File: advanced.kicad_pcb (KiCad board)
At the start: 2 copper layers, 29 parts, among them U1 ATtiny24-20P, U2 ATtiny28L-4P, U3 ATtiny13A-P, U4 ATtiny25-20P, U5 ATtiny24-20P, U6 ATtiny85-20P

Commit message: slight progres
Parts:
- removed C7: C_Polarized, Capacitor_THT:CP_Axial_L10.0mm_D4.5mm_P15.00mm_Horizontal
- added  : PinSocket_1x01_P2.54mm_Vertical, Connector_PinSocket_2.54mm:PinSocket_1x01_P2.54mm_Vertical, F.Cu at (189.9, 141.0)
- added  : PinSocket_1x01_P2.54mm_Vertical, Connector_PinSocket_2.54mm:PinSocket_1x01_P2.54mm_Vertical, F.Cu at (222.2, 141.0)
- added  : PinSocket_1x01_P2.54mm_Vertical, Connector_PinSocket_2.54mm:PinSocket_1x01_P2.54mm_Vertical, F.Cu at (163.8, 150.5)
- added  : PinSocket_1x01_P2.54mm_Vertical, Connector_PinSocket_2.54mm:PinSocket_1x01_P2.54mm_Vertical, F.Cu at (117.5, 92.7)
- added  : PinSocket_1x01_P2.54mm_Vertical, Connector_PinSocket_2.54mm:PinSocket_1x01_P2.54mm_Vertical, F.Cu at (136.5, 116.8)
- added  : PinSocket_1x01_P2.54mm_Vertical, Connector_PinSocket_2.54mm:PinSocket_1x01_P2.54mm_Vertical, F.Cu at (166.4, 136.5)
- added  : PinSocket_1x01_P2.54mm_Vertical, Connector_PinSocket_2.54mm:PinSocket_1x01_P2.54mm_Vertical, F.Cu at (101.6, 101.6)
- added  : PinSocket_1x01_P2.54mm_Vertical, Connector_PinSocket_2.54mm:PinSocket_1x01_P2.54mm_Vertical, F.Cu at (146.7, 94.0)
- added  : PinSocket_1x01_P2.54mm_Vertical, Connector_PinSocket_2.54mm:PinSocket_1x01_P2.54mm_Vertical, F.Cu at (183.5, 114.3)
- added  : PinSocket_1x01_P2.54mm_Vertical, Connector_PinSocket_2.54mm:PinSocket_1x01_P2.54mm_Vertical, F.Cu at (221.6, 94.0)
- added  : PinSocket_1x01_P2.54mm_Vertical, Connector_PinSocket_2.54mm:PinSocket_1x01_P2.54mm_Vertical, F.Cu at (233.0, 124.5)
- added  : PinSocket_1x01_P2.54mm_Vertical, Connector_PinSocket_2.54mm:PinSocket_1x01_P2.54mm_Vertical, F.Cu at (215.3, 114.3)
- added  : PinSocket_1x01_P2.54mm_Vertical, Connector_PinSocket_2.54mm:PinSocket_1x01_P2.54mm_Vertical, F.Cu at (141.0, 136.5)
- added  : PinSocket_1x01_P2.54mm_Vertical, Connector_PinSocket_2.54mm:PinSocket_1x01_P2.54mm_Vertical, F.Cu at (143.5, 130.2)
- added  : PinSocket_1x01_P2.54mm_Vertical, Connector_PinSocket_2.54mm:PinSocket_1x01_P2.54mm_Vertical, F.Cu at (128.9, 81.3)
- added  : PinSocket_1x01_P2.54mm_Vertical, Connector_PinSocket_2.54mm:PinSocket_1x01_P2.54mm_Vertical, F.Cu at (167.0, 73.7)
- added  : PinSocket_1x01_P2.54mm_Vertical, Connector_PinSocket_2.54mm:PinSocket_1x01_P2.54mm_Vertical, F.Cu at (129.5, 101.0)
- added  : PinSocket_1x01_P2.54mm_Vertical, Connector_PinSocket_2.54mm:PinSocket_1x01_P2.54mm_Vertical, F.Cu at (153.7, 136.5)
- added  : PinSocket_1x01_P2.54mm_Vertical, Connector_PinSocket_2.54mm:PinSocket_1x01_P2.54mm_Vertical, F.Cu at (101.6, 133.3)
- added  : PinSocket_1x01_P2.54mm_Vertical, Connector_PinSocket_2.54mm:PinSocket_1x01_P2.54mm_Vertical, F.Cu at (262.3, 67.3)
- added  : PinSocket_1x01_P2.54mm_Vertical, Connector_PinSocket_2.54mm:PinSocket_1x01_P2.54mm_Vertical, F.Cu at (220.3, 154.9)
- added  : PinSocket_1x01_P2.54mm_Vertical, Connector_PinSocket_2.54mm:PinSocket_1x01_P2.54mm_Vertical, F.Cu at (172.1, 116.8)
- added  : PinSocket_1x01_P2.54mm_Vertical, Connector_PinSocket_2.54mm:PinSocket_1x01_P2.54mm_Vertical, F.Cu at (192.4, 162.6)
- added  : PinSocket_1x01_P2.54mm_Vertical, Connector_PinSocket_2.54mm:PinSocket_1x01_P2.54mm_Vertical, F.Cu at (160.7, 162.6)
- added  : PinSocket_1x01_P2.54mm_Vertical, Connector_PinSocket_2.54mm:PinSocket_1x01_P2.54mm_Vertical, F.Cu at (140.3, 116.8)
- added  : PinSocket_1x01_P2.54mm_Vertical, Connector_PinSocket_2.54mm:PinSocket_1x01_P2.54mm_Vertical, F.Cu at (121.3, 160.0)
- added  : PinSocket_1x01_P2.54mm_Vertical, Connector_PinSocket_2.54mm:PinSocket_1x01_P2.54mm_Vertical, F.Cu at (178.4, 94.0)
- added  : PinSocket_1x01_P2.54mm_Vertical, Connector_PinSocket_2.54mm:PinSocket_1x01_P2.54mm_Vertical, F.Cu at (198.8, 154.9)
- added  : PinSocket_1x01_P2.54mm_Vertical, Connector_PinSocket_2.54mm:PinSocket_1x01_P2.54mm_Vertical, F.Cu at (189.9, 94.0)
- added  : PinSocket_1x01_P2.54mm_Vertical, Connector_PinSocket_2.54mm:PinSocket_1x01_P2.54mm_Vertical, F.Cu at (135.9, 150.5)
- added  : PinSocket_1x01_P2.54mm_Vertical, Connector_PinSocket_2.54mm:PinSocket_1x01_P2.54mm_Vertical, F.Cu at (150.5, 175.3)
- added  : PinSocket_1x01_P2.54mm_Vertical, Connector_PinSocket_2.54mm:PinSocket_1x01_P2.54mm_Vertical, F.Cu at (118.7, 175.3)
- added  : PinSocket_1x01_P2.54mm_Vertical, Connector_PinSocket_2.54mm:PinSocket_1x01_P2.54mm_Vertical, F.Cu at (130.2, 160.0)
- added  : PinSocket_1x01_P2.54mm_Vertical, Connector_PinSocket_2.54mm:PinSocket_1x01_P2.54mm_Vertical, F.Cu at (262.3, 80.0)
- added  : PinSocket_1x01_P2.54mm_Vertical, Connector_PinSocket_2.54mm:PinSocket_1x01_P2.54mm_Vertical, F.Cu at (108.0, 154.9)
- added  : PinSocket_1x01_P2.54mm_Vertical, Connector_PinSocket_2.54mm:PinSocket_1x01_P2.54mm_Vertical, F.Cu at (143.5, 121.3)
- added  : PinSocket_1x01_P2.54mm_Vertical, Connector_PinSocket_2.54mm:PinSocket_1x01_P2.54mm_Vertical, F.Cu at (87.6, 101.6)
- added  : PinSocket_1x01_P2.54mm_Vertical, Connector_PinSocket_2.54mm:PinSocket_1x01_P2.54mm_Vertical, F.Cu at (211.5, 124.5)
- added  : PinSocket_1x01_P2.54mm_Vertical, Connector_PinSocket_2.54mm:PinSocket_1x01_P2.54mm_Vertical, F.Cu at (137.8, 81.3)
- added  : PinSocket_1x01_P2.54mm_Vertical, Connector_PinSocket_2.54mm:PinSocket_1x01_P2.54mm_Vertical, F.Cu at (108.0, 165.1)
- added  : PinSocket_1x01_P2.54mm_Vertical, Connector_PinSocket_2.54mm:PinSocket_1x01_P2.54mm_Vertical, F.Cu at (205.1, 86.4)
- added  : PinSocket_1x01_P2.54mm_Vertical, Connector_PinSocket_2.54mm:PinSocket_1x01_P2.54mm_Vertical, F.Cu at (87.6, 133.3)
- added  : PinSocket_1x01_P2.54mm_Vertical, Connector_PinSocket_2.54mm:PinSocket_1x01_P2.54mm_Vertical, F.Cu at (103.5, 77.5)
- added  : PinSocket_1x01_P2.54mm_Vertical, Connector_PinSocket_2.54mm:PinSocket_1x01_P2.54mm_Vertical, F.Cu at (196.2, 86.4)
- added  : PinSocket_1x01_P2.54mm_Vertical, Connector_PinSocket_2.54mm:PinSocket_1x01_P2.54mm_Vertical, F.Cu at (167.0, 66.0)
- added  : PinSocket_1x01_P2.54mm_Vertical, Connector_PinSocket_2.54mm:PinSocket_1x01_P2.54mm_Vertical, F.Cu at (129.5, 132.7)
- added  : PinSocket_1x01_P2.54mm_Vertical, Connector_PinSocket_2.54mm:PinSocket_1x01_P2.54mm_Vertical, F.Cu at (212.1, 141.0)
- added  : PinSocket_1x01_P2.54mm_Vertical, Connector_PinSocket_2.54mm:PinSocket_1x01_P2.54mm_Vertical, F.Cu at (262.3, 139.7)
- added REF**: PinSocket_1x07_P2.54mm_Vertical, Connector_PinSocket_2.54mm:PinSocket_1x07_P2.54mm_Vertical, F.Cu at (141.0, 150.5)
- added REF**: PinSocket_1x02_P2.54mm_Vertical, Connector_PinSocket_2.54mm:PinSocket_1x02_P2.54mm_Vertical, F.Cu at (133.4, 136.5)
- added REF**: PinSocket_1x02_P2.54mm_Vertical, Connector_PinSocket_2.54mm:PinSocket_1x02_P2.54mm_Vertical, F.Cu at (117.5, 77.5)
- added REF**: PinSocket_1x02_P2.54mm_Vertical, Connector_PinSocket_2.54mm:PinSocket_1x02_P2.54mm_Vertical, F.Cu at (262.3, 132.1)
- added REF**: PinSocket_1x02_P2.54mm_Vertical, Connector_PinSocket_2.54mm:PinSocket_1x02_P2.54mm_Vertical, F.Cu at (262.3, 72.4)
- added REF**: PinHeader_2x15_P2.54mm_Vertical, Connector_PinHeader_2.54mm:PinHeader_2x15_P2.54mm_Vertical, B.Cu at (274.3, 158.7)
- added REF**: PinSocket_1x03_P2.54mm_Vertical, Connector_PinSocket_2.54mm:PinSocket_1x03_P2.54mm_Vertical, F.Cu at (248.3, 67.3)
- added REF**: PinSocket_1x02_P2.54mm_Vertical, Connector_PinSocket_2.54mm:PinSocket_1x02_P2.54mm_Vertical, F.Cu at (189.9, 146.1)
- added REF**: PinSocket_1x04_P2.54mm_Vertical, Connector_PinSocket_2.54mm:PinSocket_1x04_P2.54mm_Vertical, F.Cu at (248.3, 132.1)
- added REF**: PinSocket_1x04_P2.54mm_Vertical, Connector_PinSocket_2.54mm:PinSocket_1x04_P2.54mm_Vertical, F.Cu at (153.0, 66.0)
- added REF**: PinSocket_1x02_P2.54mm_Vertical, Connector_PinSocket_2.54mm:PinSocket_1x02_P2.54mm_Vertical, F.Cu at (248.3, 77.5)
- added REF**: PinSocket_1x04_P2.54mm_Vertical, Connector_PinSocket_2.54mm:PinSocket_1x04_P2.54mm_Vertical, F.Cu at (103.5, 82.5)
- added REF**: PinSocket_1x02_P2.54mm_Vertical, Connector_PinSocket_2.54mm:PinSocket_1x02_P2.54mm_Vertical, F.Cu at (146.1, 136.5)
- added REF**: PinSocket_1x04_P2.54mm_Vertical, Connector_PinSocket_2.54mm:PinSocket_1x04_P2.54mm_Vertical, F.Cu at (203.8, 141.0)
- moved R11 141.7 mm to (279.4, 86.4), turned to -90 degrees
- moved D1 108.7 mm to (108.0, 158.8), turned to -90 degrees
- moved R6 96.3 mm to (87.6, 104.8), turned to -90 degrees
- moved R10 90.2 mm to (236.2, 64.8), turned to 90 degrees
- moved C8 86.9 mm to (246.6, 111.6), turned to 90 degrees
- moved U1 78.1 mm to (106.7, 77.5)
- moved C2 77.0 mm to (124.5, 160.0)
- moved D4 72.1 mm to (275.6, 67.3)
- moved C5 71.9 mm to (202.1, 154.9)
- moved C6 71.8 mm to (214.8, 124.5)
- moved R3 69.3 mm to (147.3, 175.3), turned to 180 degrees
- moved U5 67.8 mm to (259.1, 80.0), turned to 180 degrees
- moved U2 65.8 mm to (133.4, 147.3), turned to 90 degrees
- moved U3 60.2 mm to (156.2, 66.0)
- moved R1 56.8 mm to (101.6, 104.8), turned to -90 degrees
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
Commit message: a
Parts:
- added  : PinSocket_1x01_P2.54mm_Vertical, Connector_PinSocket_2.54mm:PinSocket_1x01_P2.54mm_Vertical, F.Cu at (281.9, 67.3)
- added  : PinSocket_1x01_P2.54mm_Vertical, Connector_PinSocket_2.54mm:PinSocket_1x01_P2.54mm_Vertical, F.Cu at (279.4, 104.8)
- added  : PinSocket_1x01_P2.54mm_Vertical, Connector_PinSocket_2.54mm:PinSocket_1x01_P2.54mm_Vertical, F.Cu at (246.4, 114.9)
- added  : PinSocket_1x01_P2.54mm_Vertical, Connector_PinSocket_2.54mm:PinSocket_1x01_P2.54mm_Vertical, F.Cu at (236.2, 67.9)
- added  : PinSocket_1x01_P2.54mm_Vertical, Connector_PinSocket_2.54mm:PinSocket_1x01_P2.54mm_Vertical, F.Cu at (209.6, 66.0)
- added  : PinSocket_1x01_P2.54mm_Vertical, Connector_PinSocket_2.54mm:PinSocket_1x01_P2.54mm_Vertical, F.Cu at (246.4, 93.3)
- added  : PinSocket_1x01_P2.54mm_Vertical, Connector_PinSocket_2.54mm:PinSocket_1x01_P2.54mm_Vertical, F.Cu at (236.2, 46.4)
- added  : PinSocket_1x01_P2.54mm_Vertical, Connector_PinSocket_2.54mm:PinSocket_1x01_P2.54mm_Vertical, F.Cu at (271.8, 67.3)
- added  : PinSocket_1x01_P2.54mm_Vertical, Connector_PinSocket_2.54mm:PinSocket_1x01_P2.54mm_Vertical, F.Cu at (279.4, 83.2)
- added  : PinSocket_1x01_P2.54mm_Vertical, Connector_PinSocket_2.54mm:PinSocket_1x01_P2.54mm_Vertical, F.Cu at (199.4, 66.0)
- R1, R10, R11, R2, R3, R4, R5, R6, R7, R8, R9: footprint Resistor_THT:R_Axial_DIN0309_L9.0mm_D3.2mm_P25.40mm_Horizontal -> Resistor_THT:R_Axial_DIN0309_L9.0mm_D3.2mm_P15.24mm_Horizontal
- moved   45.2 mm to (149.2, 175.9)
- moved   43.8 mm to (106.7, 175.9)
- moved R3 43.8 mm to (103.5, 175.9)
- moved   41.2 mm to (62.2, 134.0)
- moved R6 41.2 mm to (62.2, 137.2)
- moved U2 36.4 mm to (99.7, 161.3)
- moved   36.4 mm to (130.2, 164.5)
- moved   36.4 mm to (132.7, 150.5)
- moved   36.4 mm to (107.3, 150.5)
- moved REF** 36.4 mm to (107.3, 164.5)
- moved REF** 36.4 mm to (99.7, 150.5)
- moved   36.4 mm to (120.0, 150.5)
- moved   36.4 mm to (102.2, 164.5)
- moved REF** 36.4 mm to (112.4, 150.5)
- moved R8 35.6 mm to (130.8, 175.9)
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
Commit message: pathing done
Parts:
- removed the   at (138.4, 109.9)
- removed the   at (120.0, 150.5)
- added  : PinSocket_1x01_P2.54mm_Vertical, Connector_PinSocket_2.54mm:PinSocket_1x01_P2.54mm_Vertical, F.Cu at (118.1, 125.1)
- added  : PinSocket_1x01_P2.54mm_Vertical, Connector_PinSocket_2.54mm:PinSocket_1x01_P2.54mm_Vertical, F.Cu at (131.1, 129.0)
- added REF**: PinSocket_1x06_P2.54mm_Vertical, Connector_PinSocket_2.54mm:PinSocket_1x06_P2.54mm_Vertical, F.Cu at (189.9, 154.3)
- added REF**: PinSocket_1x06_P2.54mm_Vertical, Connector_PinSocket_2.54mm:PinSocket_1x06_P2.54mm_Vertical, F.Cu at (133.3, 56.5)
- moved REF** 64.0 mm to (104.8, 87.0)
- moved   52.0 mm to (144.8, 113.7), turned to -90 degrees
- moved   50.4 mm to (104.1, 106.0)
- moved   50.4 mm to (104.1, 127.6)
- moved R6 50.4 mm to (104.1, 109.2)
- moved C2 47.7 mm to (144.8, 116.8), turned to -90 degrees
- moved   44.7 mm to (235.6, 113.7)
- moved   44.7 mm to (235.6, 92.1)
- moved R11 44.7 mm to (235.6, 95.2)
- moved REF** 40.9 mm to (245.7, 129.5)
- moved   40.2 mm to (144.8, 122.6), turned to -90 degrees
- moved   38.1 mm to (247.0, 82.5), turned to -90 degrees
- moved U6 37.6 mm to (214.6, 124.5)
- moved REF** 37.6 mm to (225.4, 124.5)
- moved REF** 37.6 mm to (211.5, 124.5)
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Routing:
- net (no net): track 0.00 -> 2318.0 mm
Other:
- board text added: "GND"
- board text added: "VCC"

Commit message: control components connected
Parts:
- added LED: LED_D5.0mm, LED_THT:LED_D5.0mm, F.Cu at (241.3, 129.5)
- added PIEZO: Buzzer_TDK_PS1240P02BT_D12.2mm_H6.5mm, Buzzer_Beeper:Buzzer_TDK_PS1240P02BT_D12.2mm_H6.5mm, F.Cu at (255.3, 116.3)
- added R (LED): R_Axial_DIN0207_L6.3mm_D2.5mm_P10.16mm_Horizontal, Resistor_THT:R_Axial_DIN0207_L6.3mm_D2.5mm_P10.16mm_Horizontal, F.Cu at (251.5, 134.6)
- added R (PIEZO): R_Axial_DIN0207_L6.3mm_D2.5mm_P10.16mm_Horizontal, Resistor_THT:R_Axial_DIN0207_L6.3mm_D2.5mm_P10.16mm_Horizontal, F.Cu at (264.4, 133.6)
- added RESET: SW_PUSH_6mm_H8.5mm, Button_Switch_THT:SW_PUSH_6mm_H8.5mm, F.Cu at (253.0, 127.8)
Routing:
- net (no net): track 2318.0 -> 2409.2 mm
- net Net-(D4-Pad1): track 0.00 -> 8.58 mm
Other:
- board text added: "+"
- board text added: "-"
- board text added: "ADVANCED"
- board text added: "BOMB ADVANCED"
- board text added: "by phuid & Milda"

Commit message: Add files via upload
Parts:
- moved RESET 5.27 mm to (257.5, 125.0), turned to -90 degrees
- moved PIEZO 4.96 mm to (260.2, 115.6), turned to 180 degrees
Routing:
- net (no net): track 2409.2 -> 2349.1 mm

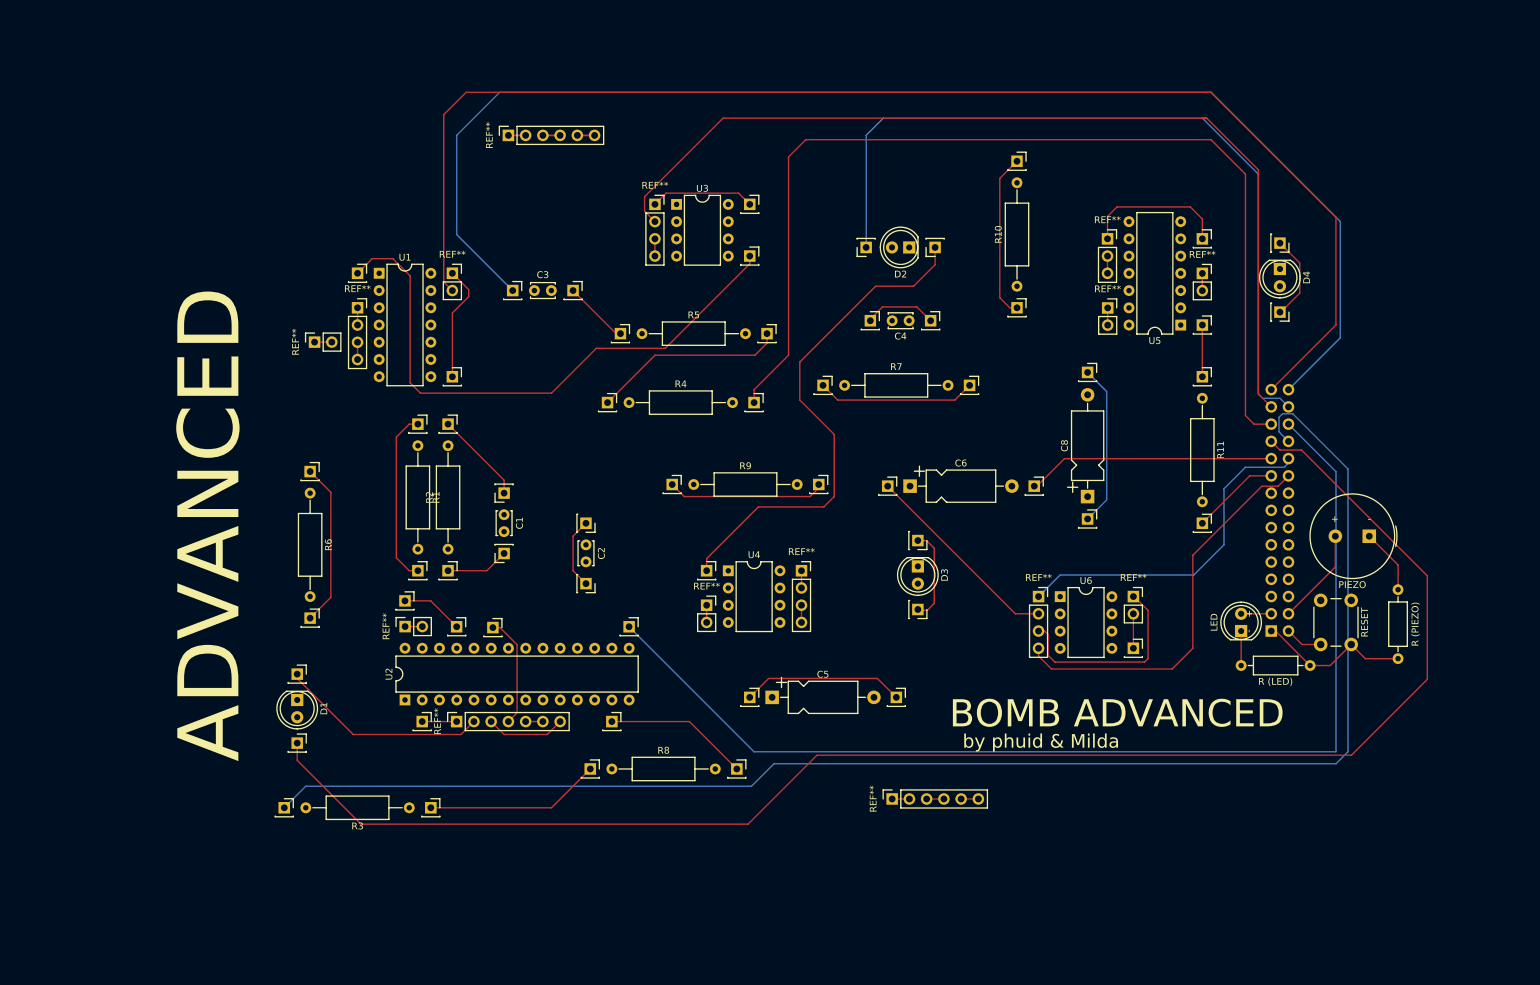
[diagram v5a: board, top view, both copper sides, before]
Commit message: potencio added, not 100% sure, cleanup, clarity changes
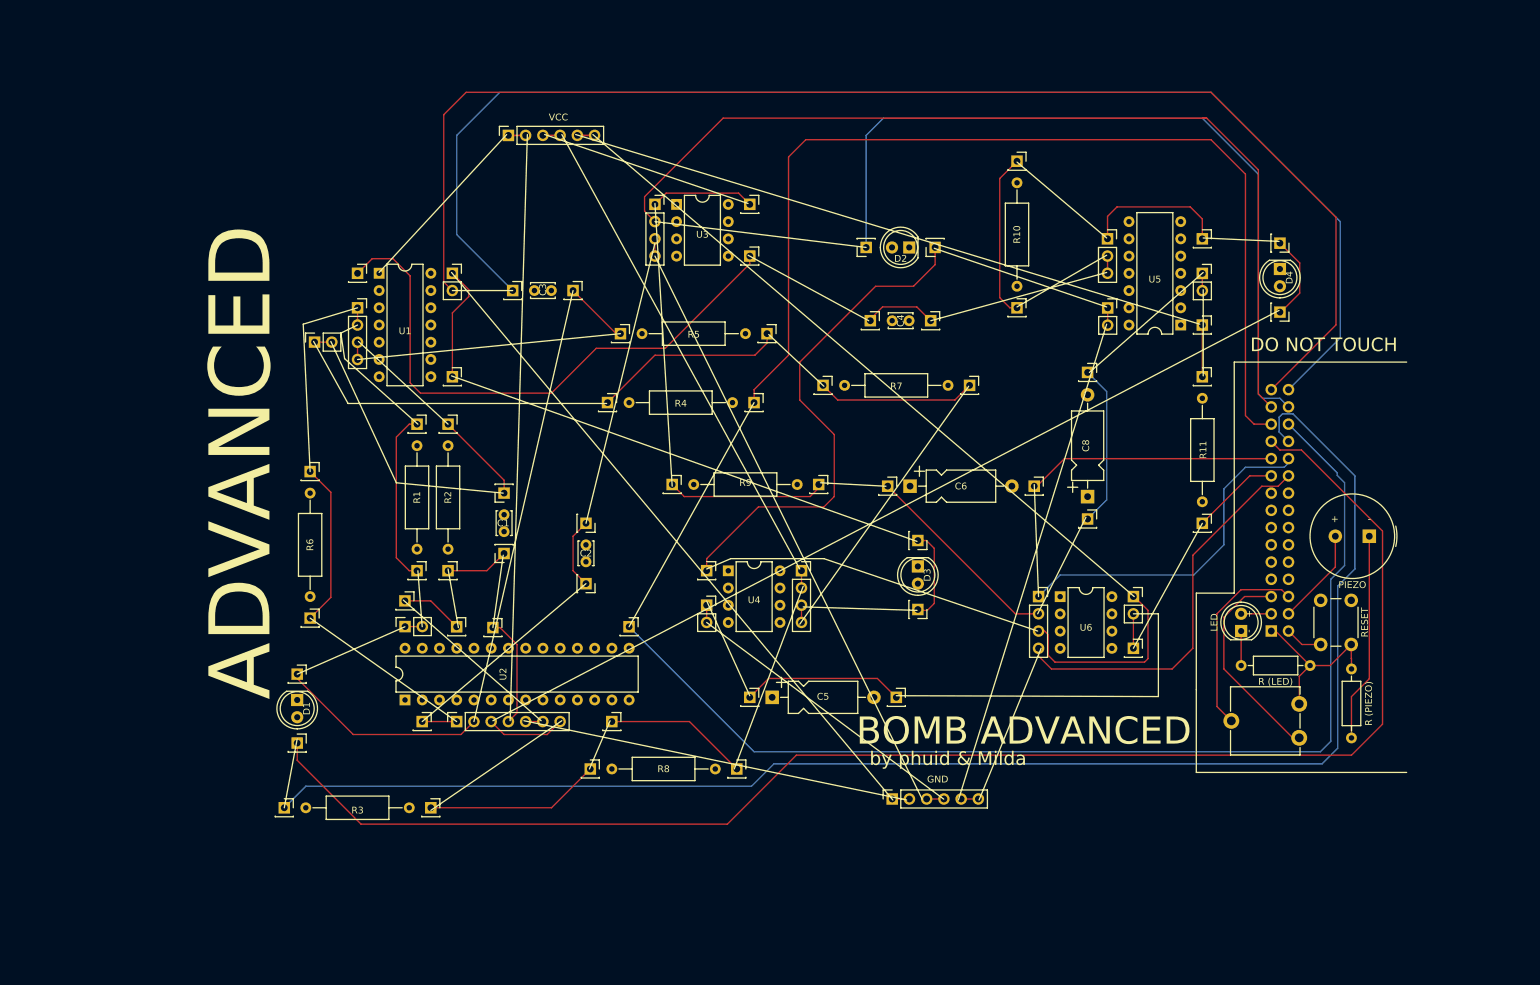
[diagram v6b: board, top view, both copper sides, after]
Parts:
- added REF**: Potentiometer_ACP_CA9-V10_Vertical, Potentiometer_THT:Potentiometer_ACP_CA9-V10_Vertical, F.Cu at (249.9, 140.3)
- moved R (PIEZO) 13.5 mm to (257.6, 145.3)
- moved   0.13 mm to (119.9, 99.1)
- moved   0.13 mm to (119.9, 120.7)
- moved R1 0.13 mm to (119.9, 102.2)
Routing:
- net (no net): track 2349.1 -> 2426.6 mm
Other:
- board text added: "DO NOT TOUCH"
